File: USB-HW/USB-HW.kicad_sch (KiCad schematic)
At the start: 0 parts

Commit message: feat: Add USB input section
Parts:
- added J1: USB A, symbol USB-HW:USB_A-Connector
- added U1: SP0503BAHTG, symbol USB-HW:TVS_ARR
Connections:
- new net D_N: J1.2 (D-), U1.3 (I/O_2)
- new net D_P: J1.3 (D+), U1.4 (I/O_3)
- new net GND: J1.4 (GND), U1.1 (GND)
- new net VBUS: J1.1 (VBUS), U1.2 (I/O_1)
- no-connect marks 0 -> 2
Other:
- note added: "USB input"

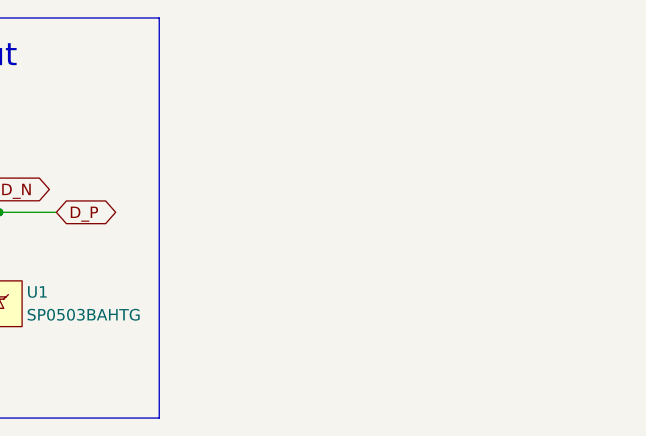
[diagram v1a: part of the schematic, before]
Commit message: feat: Add PI filter section
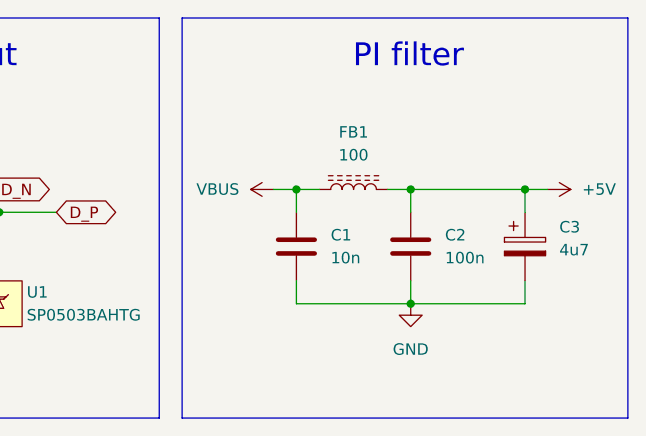
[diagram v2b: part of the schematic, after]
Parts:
- added C1: 10n, symbol Device:C
- added C2: 100n, symbol Device:C
- added C3: 4u7, symbol Device:C_Polarized
- added FB1: 100, symbol Device:L_Ferrite
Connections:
- net GND: now also C1.2, C2.2, C3.2
- net VBUS: now also C1.1, FB1.1
- new net +5V: C2.1, C3.1, FB1.2
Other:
- note added: "PI filter"

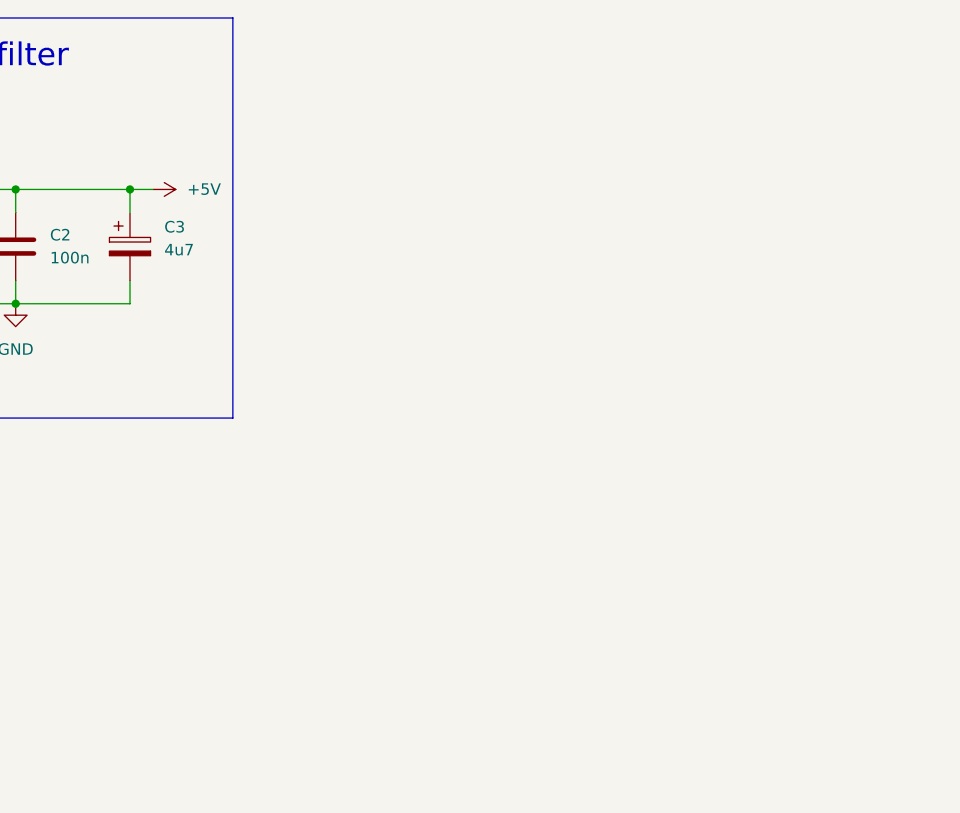
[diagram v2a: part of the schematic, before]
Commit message: feat: Add bridge section
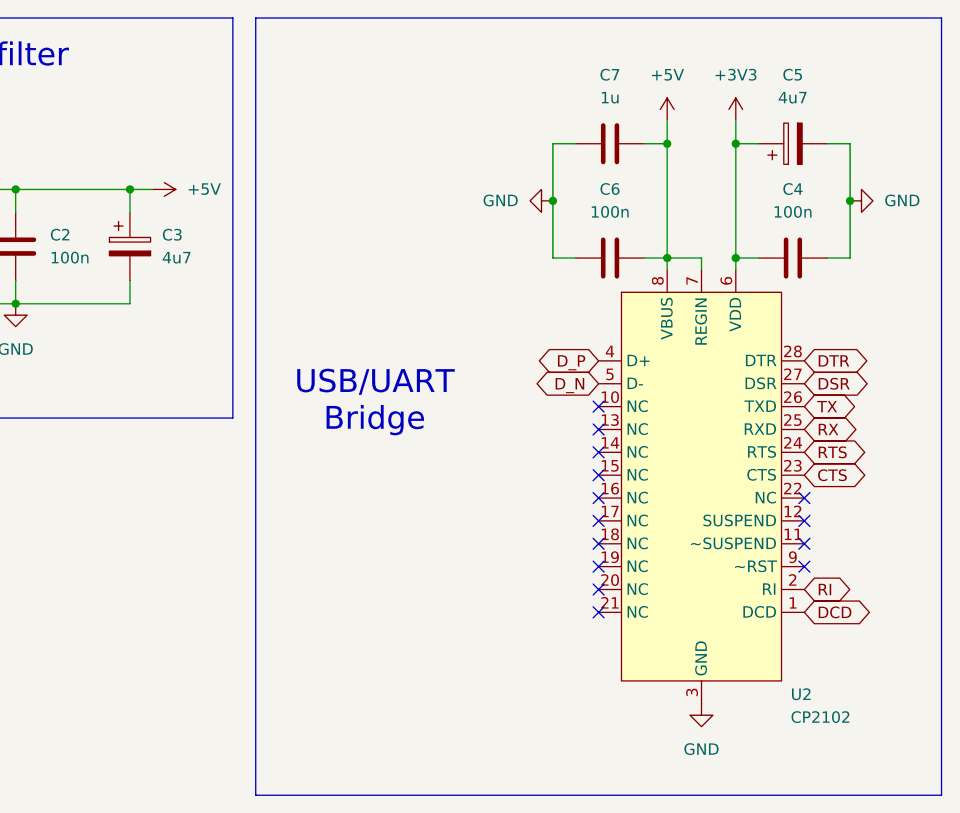
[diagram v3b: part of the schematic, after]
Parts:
- added C4, C6: 100n, symbol Device:C
- added C5: 4u7, symbol Device:C_Polarized
- added C7: 1u, symbol Device:C
- added U2: CP2102, symbol USB-HW:CP2102
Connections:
- net +5V: now also C6.1, C7.1, U2.7 (REGIN), U2.8 (VBUS)
- net D_N: now also U2.5 (D-)
- net D_P: now also U2.4 (D+)
- net GND: now also C4.1, C5.2, C6.2, C7.2, U2.3 (GND)
- new net +3V3: C4.2, C5.1, U2.6 (VDD)
- new net CTS: U2.23 (CTS)
- new net DCD: U2.1 (DCD)
- new net DSR: U2.27 (DSR)
- new net DTR: U2.28 (DTR)
- new net RI: U2.2 (RI)
- new net RTS: U2.24 (RTS)
- new net RX: U2.25 (RXD)
- new net TX: U2.26 (TXD)
- no-connect marks 2 -> 16
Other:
- note added: "USB/UART Bridge"

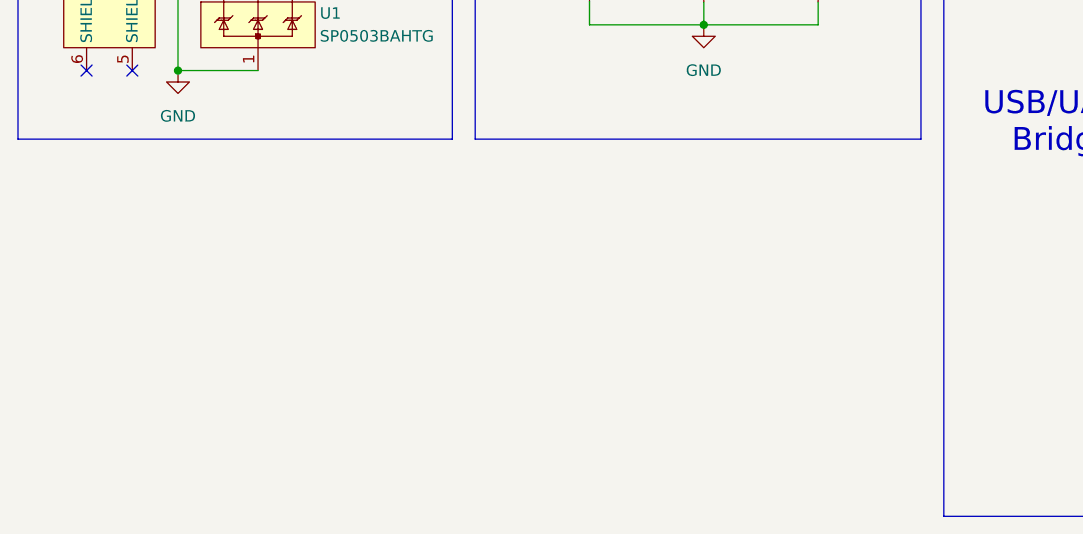
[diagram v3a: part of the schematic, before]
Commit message: feat: Add indicators section
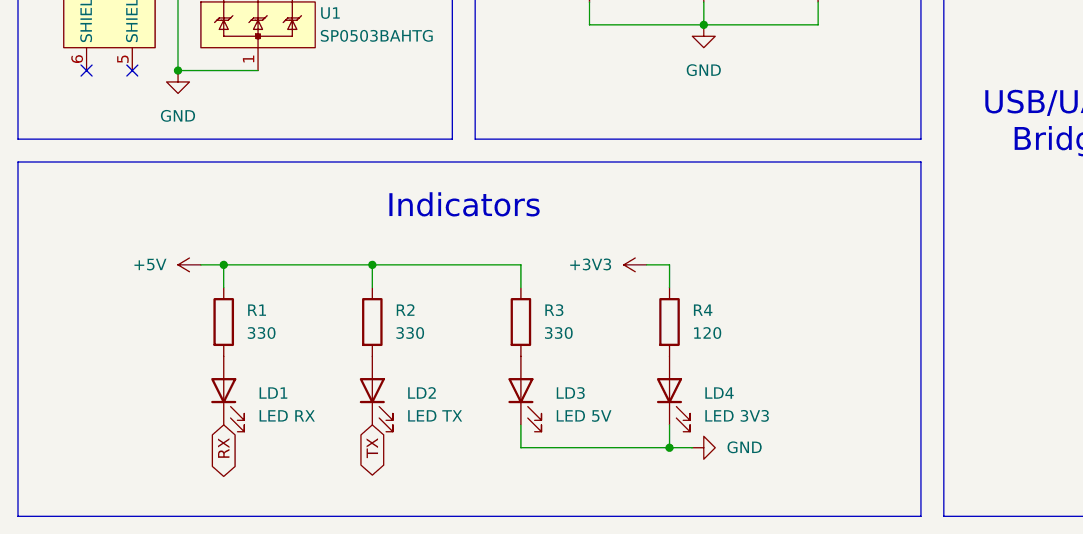
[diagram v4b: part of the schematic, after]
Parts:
- added LD1: LED RX, symbol Device:LED
- added LD2: LED TX, symbol Device:LED
- added LD3: LED 5V, symbol Device:LED
- added LD4: LED 3V3, symbol Device:LED
- added R1, R2, R3: 330, symbol Device:R
- added R4: 120, symbol Device:R
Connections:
- net +3V3: now also R4.1
- net +5V: now also R1.1, R2.1, R3.1
- net GND: now also LD3.1 (K), LD4.1 (K)
- net RX: now also LD1.1 (K)
- net TX: now also LD2.1 (K)
- new net: LD1.2 (A), R1.2
- new net: LD2.2 (A), R2.2
- new net: LD4.2 (A), R4.2
- new net: LD3.2 (A), R3.2
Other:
- note added: "Indicators"

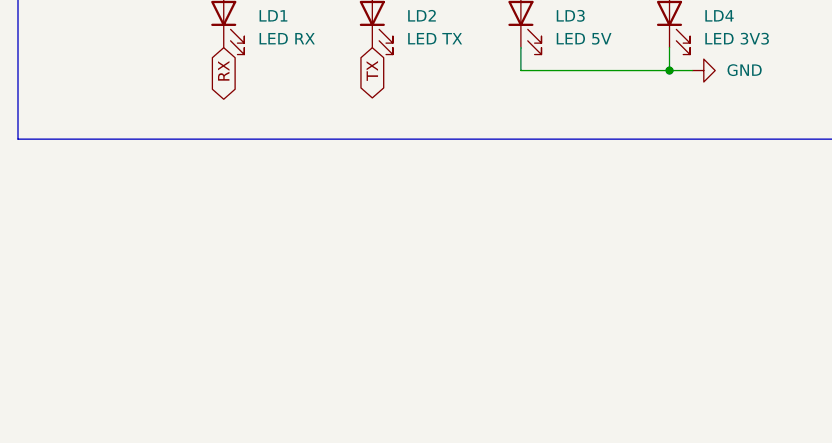
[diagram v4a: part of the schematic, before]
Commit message: feat: Add interfaces section
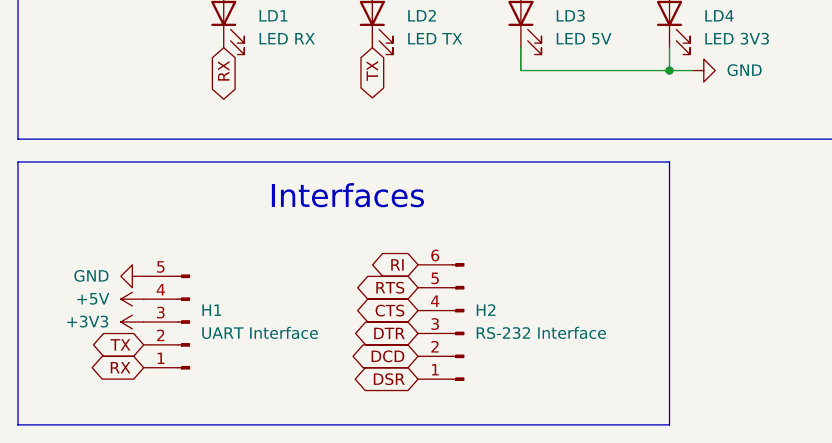
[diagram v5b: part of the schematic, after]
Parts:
- added H1: UART Interface, symbol Connector:Conn_01x05_Pin
- added H2: RS-232 Interface, symbol Connector:Conn_01x06_Pin
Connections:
- net +3V3: now also H1.3 (Pin_3)
- net +5V: now also H1.4 (Pin_4)
- net CTS: now also H2.4 (Pin_4)
- net DCD: now also H2.2 (Pin_2)
- net DSR: now also H2.1 (Pin_1)
- net DTR: now also H2.3 (Pin_3)
- net GND: now also H1.5 (Pin_5)
- net RI: now also H2.6 (Pin_6)
- net RTS: now also H2.5 (Pin_5)
- net RX: now also H1.1 (Pin_1)
- net TX: now also H1.2 (Pin_2)
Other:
- note added: "Interfaces"

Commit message: feat: Add footprints
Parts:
- C1, C2, C4, C6, C7: footprint (none) -> Capacitor_SMD:C_0805_2012Metric
- C3, C5: footprint (none) -> Capacitor_SMD:CP_Elec_4x5.3
- FB1: footprint (none) -> Inductor_SMD:L_0805_2012Metric
- H1: footprint (none) -> Connector_PinHeader_2.54mm:PinHeader_1x05_P2.54mm_Vertical
- H2: footprint (none) -> Connector_PinSocket_2.54mm:PinSocket_1x06_P2.54mm_Vertical
- J1: footprint (none) -> Connector_USB:USB_A_Molex_48037-2200_Horizontal
- LD1, LD2, LD3, LD4: footprint (none) -> LED_SMD:LED_0805_2012Metric
- R1, R2, R3, R4: footprint (none) -> Resistor_SMD:R_0805_2012Metric
- U1: footprint (none) -> Package_TO_SOT_SMD:SOT-143
- U2: footprint (none) -> Package_DFN_QFN:QFN-28-1EP_5x5mm_P0.5mm_EP3.25x3.25mm
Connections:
- net GND: now also U2.29 (EP)
- no-connect marks 16 -> 15
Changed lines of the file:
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@@
 	)
 	(junction
+		(at 167.64 92.71)
+		(diameter 0)
+		(color 0 0 0 0)
+	)
+	(junction
 		(at 45.72 36.83)
 		(diameter 0)
@@
 	)
 	(no_connect
-		(at 27.94 52.07)
+		(at 25.4 52.07)
 	)
 	(no_connect
@@
 	)
 	(no_connect
-		(at 22.86 52.07)
-	)
-	(no_connect
 		(at 156.21 66.04)
 	)
@@
 	(wire
 		(pts
+			(xy 170.18 92.71) (xy 170.18 91.44)
+		)
+		(stroke
+			(width 0)
+			(type default)
+		)
+	)
+	(wire
+		(pts
 			(xy 71.12 73.66) (xy 71.12 76.2)
 		)
@@
 	(wire
 		(pts
+			(xy 165.1 92.71) (xy 165.1 91.44)
+		)
+		(stroke
+			(width 0)
+			(type default)
+		)
+	)
+	(wire
+		(pts
 			(xy 90.17 93.98) (xy 87.63 93.98)
 		)
@@
 	(wire
 		(pts
+			(xy 167.64 92.71) (xy 170.18 92.71)
+		)
+		(stroke
+			(width 0)
+			(type default)
+		)
+	)
+	(wire
+		(pts
 			(xy 104.14 36.83) (xy 104.14 34.29)
 		)
@@
 	(wire
 		(pts
+			(xy 167.64 92.71) (xy 165.1 92.71)
+		)
+		(stroke
+			(width 0)
+			(type default)
+		)
+	)
+	(wire
+		(pts
 			(xy 161.29 41.91) (xy 163.83 41.91)
 		)
@@
 			)
 		)
-		(property "Footprint" ""
+		(property "Footprint" "Resistor_SMD:R_0805_2012Metric"
 			(at 36.322 80.01 90)
 			(effects
@@
 			)
 		)
-		(property "Footprint" ""
+		(property "Footprint" "Connector_PinSocket_2.54mm:PinSocket_1x06_P2.54mm_Vertical"
 			(at 64.77 123.19 0)
 			(effects
@@
 			)
 		)
-		(property "Footprint" ""
+		(property "Footprint" "Resistor_SMD:R_0805_2012Metric"
 			(at 52.832 80.01 90)
 			(effects
@@
 			)
 		)
-		(property "Footprint" ""
+		(property "Footprint" "Capacitor_SMD:C_0805_2012Metric"
 			(at 153.67 42.8752 0)
 			(effects
@@
 			)
 		)
-		(property "Footprint" ""
+		(property "Footprint" "Capacitor_SMD:CP_Elec_4x5.3"
 			(at 105.1052 44.45 0)
 			(effects
@@
 			)
 		)
-		(property "Footprint" ""
+		(property "Footprint" "Resistor_SMD:R_0805_2012Metric"
 			(at 85.852 80.01 90)
 			(effects
@@
 			)
 		)
-		(property "Footprint" ""
+		(property "Footprint" "Capacitor_SMD:CP_Elec_4x5.3"
 			(at 181.61 28.2448 0)
 			(effects
@@
 			)
 		)
-		(property "Footprint" ""
+		(property "Footprint" "Capacitor_SMD:C_0805_2012Metric"
 			(at 92.4052 44.45 0)
 			(effects
@@
 	(symbol
 		(lib_id "power:GND")
-		(at 167.64 91.44 0)
+		(at 167.64 92.71 0)
 		(unit 1)
 		(exclude_from_sim no)
@@
 		(fields_autoplaced yes)
 		(property "Reference" "#PWR06"
-			(at 167.64 97.79 0)
+			(at 167.64 99.06 0)
 			(effects
 				(font
@@
 		)
 		(property "Value" "GND"
-			(at 167.64 96.52 0)
+			(at 167.64 97.79 0)
 			(effects
 				(font
@@
 		)
 		(property "Footprint" ""
-			(at 167.64 91.44 0)
+			(at 167.64 92.71 0)
 			(effects
 				(font
@@
 		)
 		(property "Datasheet" ""
-			(at 167.64 91.44 0)
+			(at 167.64 92.71 0)
 			(effects
 				(font
@@
 		)
 		(property "Description" "Power symbol creates a global label with name \"GND\" , ground"
-			(at 167.64 91.44 0)
+			(at 167.64 92.71 0)
 			(effects
 				(font
@@
 			)
 		)
-		(property "Footprint" ""
+		(property "Footprint" "Capacitor_SMD:C_0805_2012Metric"
 			(at 153.67 30.1752 0)
 			(effects
@@
 			)
 		)
-		(property "Footprint" ""
+		(property "Footprint" "LED_SMD:LED_0805_2012Metric"
 			(at 54.61 87.63 0)
 			(effects
@@
 			)
 		)
-		(property "Footprint" ""
+		(property "Footprint" "Package_TO_SOT_SMD:SOT-143"
 			(at 41.91 46.99 0)
 			(effects
@@
 			)
 		)
-		(property "Footprint" ""
+		(property "Footprint" "Connector_USB:USB_A_Molex_48037-2200_Horizontal"
 			(at 25.4 39.37 0)
 			(effects
@@
 		(pin "1"
 		)
-		(pin "6"
-		)
 		(pin "3"
 		)
@@
 			)
 		)
-		(property "Footprint" ""
+		(property "Footprint" "LED_SMD:LED_0805_2012Metric"
 			(at 87.63 87.63 0)
 			(effects
@@
 			)
 		)
-		(property "Footprint" ""
+		(property "Footprint" "Capacitor_SMD:C_0805_2012Metric"
 			(at 173.99 42.8752 0)
 			(effects
@@
 			)
 		)
-		(property "Footprint" ""
+		(property "Footprint" "Inductor_SMD:L_0805_2012Metric"
 			(at 85.09 34.29 0)
 			(effects
@@
 			)
 		)
-		(property "Footprint" ""
+		(property "Footprint" "Package_DFN_QFN:QFN-28-1EP_5x5mm_P0.5mm_EP3.25x3.25mm"
 			(at 167.64 64.77 0)
 			(effects
@@
 		(pin "18"
 		)
+		(pin "29"
+		)
 		(instances
 			(project ""
@@
 			)
 		)
-		(property "Footprint" ""
+		(property "Footprint" "Connector_PinHeader_2.54mm:PinHeader_1x05_P2.54mm_Vertical"
 			(at 34.29 121.92 0)
 			(effects
@@
 			)
 		)
-		(property "Footprint" ""
+		(property "Footprint" "LED_SMD:LED_0805_2012Metric"
 			(at 71.12 87.63 0)
 			(effects
@@
 			)
 		)
-		(property "Footprint" ""
+		(property "Footprint" "Capacitor_SMD:C_0805_2012Metric"
 			(at 79.7052 44.45 0)
 			(effects
@@
 			)
 		)
-		(property "Footprint" ""
+		(property "Footprint" "LED_SMD:LED_0805_2012Metric"
 			(at 38.1 87.63 0)
 			(effects
@@
 			)
 		)
-		(property "Footprint" ""
+		(property "Footprint" "Resistor_SMD:R_0805_2012Metric"
 			(at 69.342 80.01 90)
 			(effects
